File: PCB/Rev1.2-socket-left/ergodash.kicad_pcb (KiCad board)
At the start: 2 copper layers, 149.9 x 127.4 mm, 83 parts, among them J1 5PIN, SW1 SW_PUSH, SW10 SW_PUSH, SW11 SW_PUSH, SW12 SW_PUSH, SW13 SW_PUSH, SW14 SW_PUSH, SW15 SW_PUSH, SW16 SW_PUSH, SW17 SW_PUSH, SW18 SW_PUSH, SW19 SW_PUSH, SW2 SW_PUSH, SW20 SW_PUSH, SW21 SW_PUSH, SW22 SW_PUSH, SW23 SW_PUSH, SW24 SW_PUSH, SW25 SW_PUSH, SW26 SW_PUSH, SW27 SW_PUSH, SW28 SW_PUSH, SW29 SW_Push, SW3 SW_PUSH, SW30 SW_PUSH, SW31 SW_PUSH, SW32 SW_PUSH, SW33 SW_PUSH, SW34 SW_PUSH, SW35 SW_PUSH, SW4 SW_PUSH, SW40 SW_PUSH, SW5 SW_PUSH, SW6 SW_PUSH, SW7 SW_PUSH, SW8 SW_PUSH, SW9 SW_PUSH, U1 HOLE, U2 HOLE, U3 ProMicro, U4 HOLE, U5 HOLE, U7 HOLE, U8 HOLE, U9 HOLE

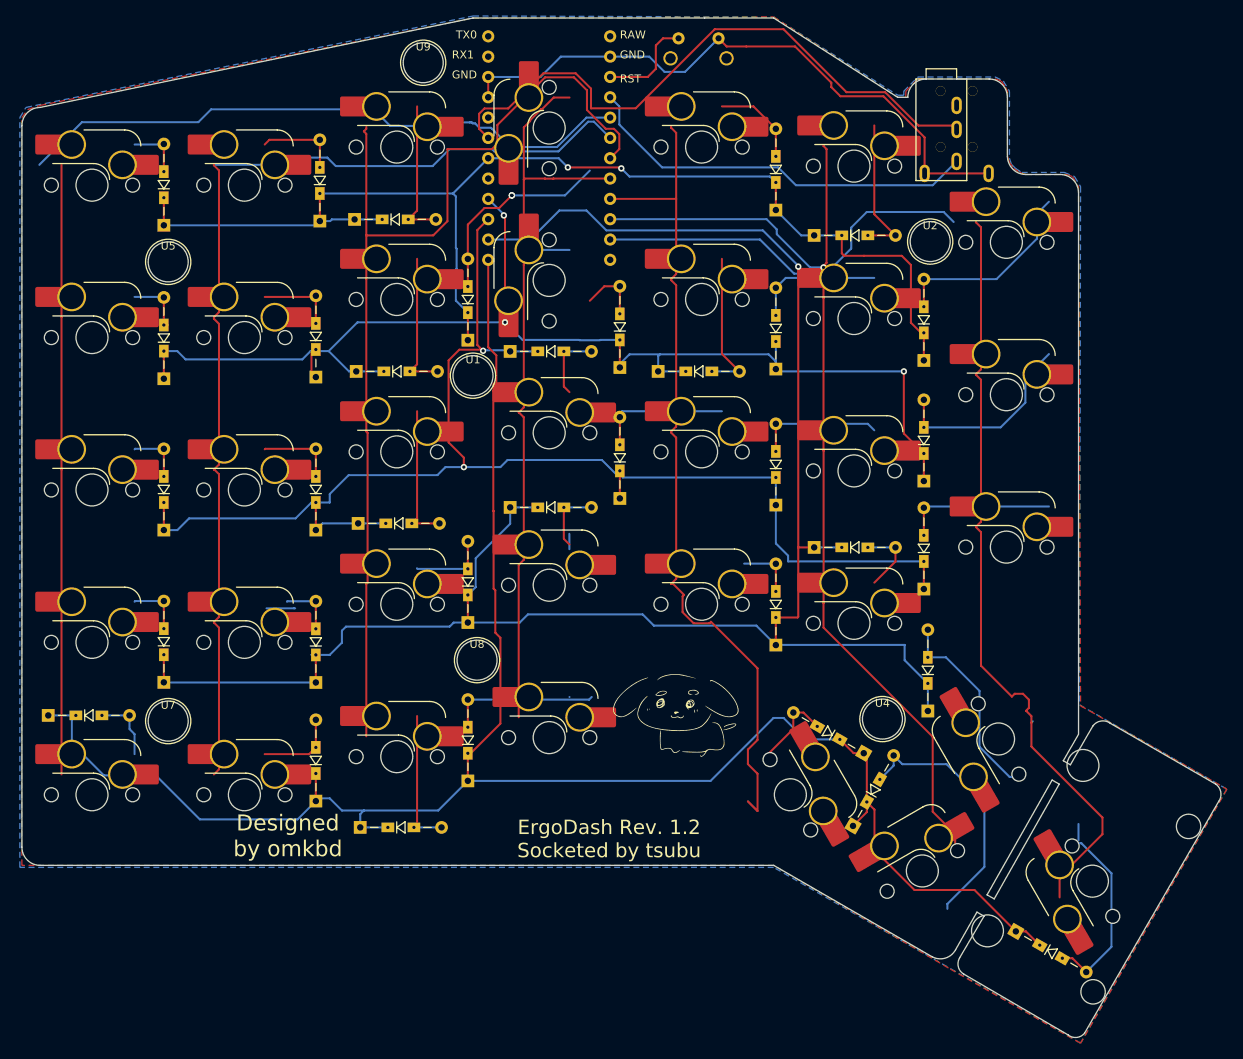
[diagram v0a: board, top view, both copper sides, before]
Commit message: Swap socket-left/right dirs to match the actual hand
The board in Rev1.2-socket-left actually builds the RIGHT hand and vice versa:
the components/sockets sit on F.Cu, which per the build guide is the underside
(裏側), so the KiCad layout is the bottom view -- mirror-reversed from use. The
inner-edge features (TRRS J1, 2U thumb SW40) are on +X, which maps to the left in
use = a right-hand half.

Swapped the two directories' contents and fixed the title blocks accordingly:
  Rev1.2-socket-right <- the active flipped-socket board (right hand, has the
                         in-progress routing)
  Rev1.2-socket-left  <- the old stale flip (NOTE: still a right-hand board, not
                         a valid left hand; to be replaced by a real left layout)

Co-Authored-By: Claude Opus 4.8 <noreply@anthropic.com>
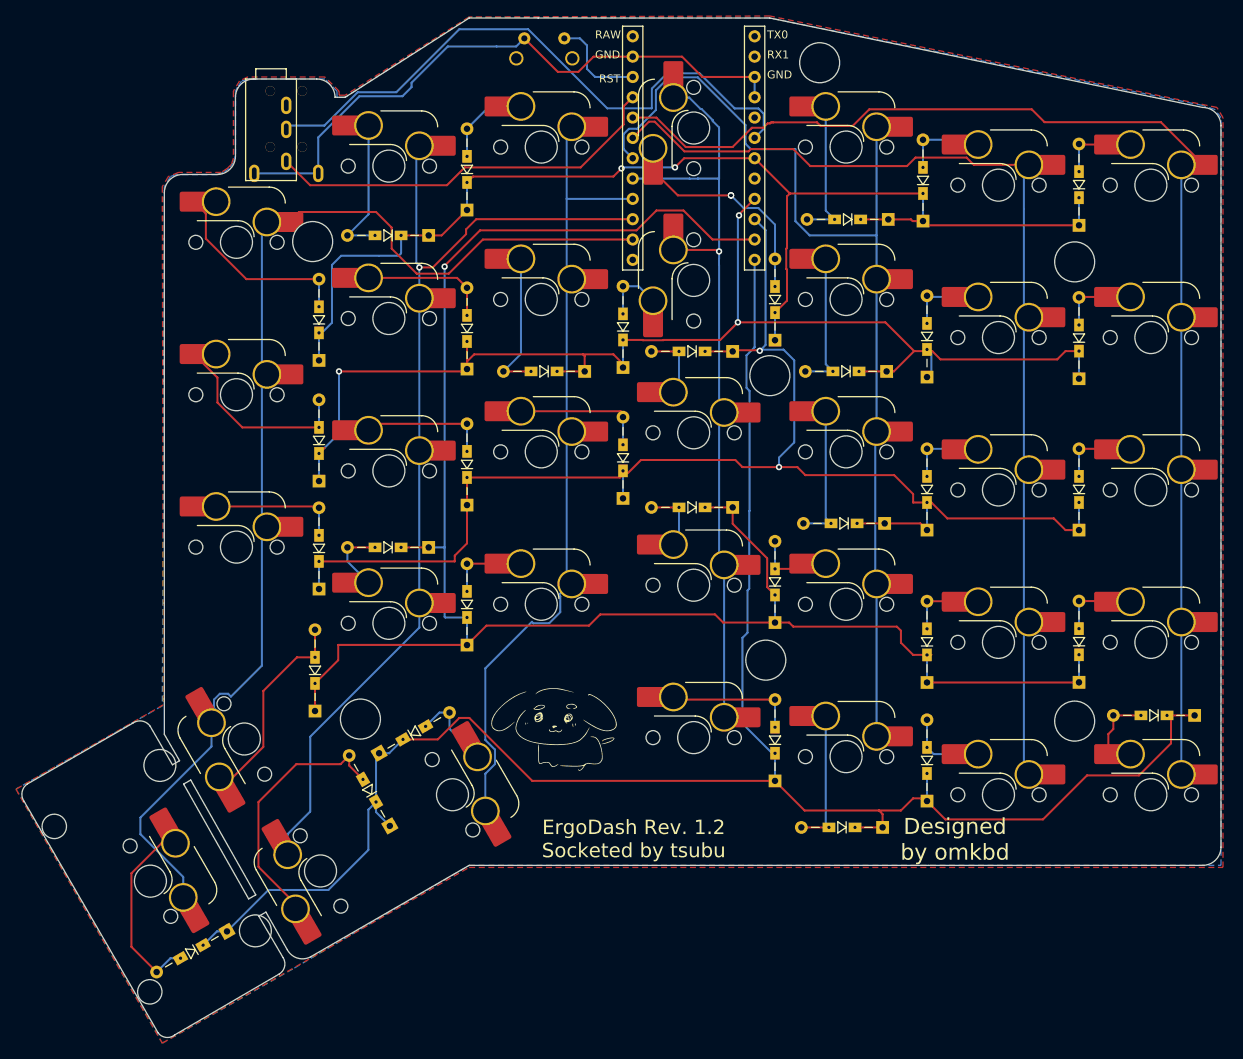
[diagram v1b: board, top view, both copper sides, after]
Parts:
- ?: moved to F.Cu
- ? (x2), D1, D10, D11, D12, D13, D14, D15, D16, D17, D18, D19, D2, D20, D21, D22, D23, D24, D25, D26, D27, D28, D29, D3, D30, D31, D32, D33, D34, D4, D5, D6, D68, D7, D8, D9, J1, SW29, U1, U2, U3, U4, U5, U7, U8, U9: moved to B.Cu
- moved D29 143.3 mm to (224.8, 124.3), turned to 180 degrees
- moved SW1 132.4 mm to (219.4, 58.0)
- moved SW2 132.4 mm to (219.4, 77.0)
- moved SW3 132.4 mm to (219.4, 96.1)
- moved SW30 132.4 mm to (219.4, 134.2)
- moved SW4 132.4 mm to (219.4, 115.1)
- moved ? 117.8 mm to (94.3, 145.0), turned to -60 degrees
- moved SW40 117.8 mm to (94.3, 145.0), turned to 120 degrees
- moved D1 114.4 mm to (210.4, 63.0)
- moved D2 114.4 mm to (210.4, 82.2)
- moved D3 114.4 mm to (210.4, 101.1)
- moved D4 114.4 mm to (210.4, 120.1)
- moved U5 113.3 mm to (209.8, 67.6), turned to 180 degrees
- moved U7 113.3 mm to (209.8, 125.0), turned to 180 degrees
- moved D68 98.6 mm to (103.9, 151.3), turned to -150 degrees
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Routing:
- net /col1: track 136.2 -> 132.6 mm
- net Net-(D8-A): track 7.09 -> 10.7 mm
- added copper zone on B.Cu, net GND
- added copper zone on F.Cu, net VCC
- removed copper zone on F.Cu, net GND
- removed copper zone on B.Cu, net VCC
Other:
- outline, holes or cut-outs redrawn
